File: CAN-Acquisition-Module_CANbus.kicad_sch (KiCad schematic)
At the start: 20 parts, among them J5 OSTVN04A150, J6 OSTVN04A150, U4 SN65HVD234

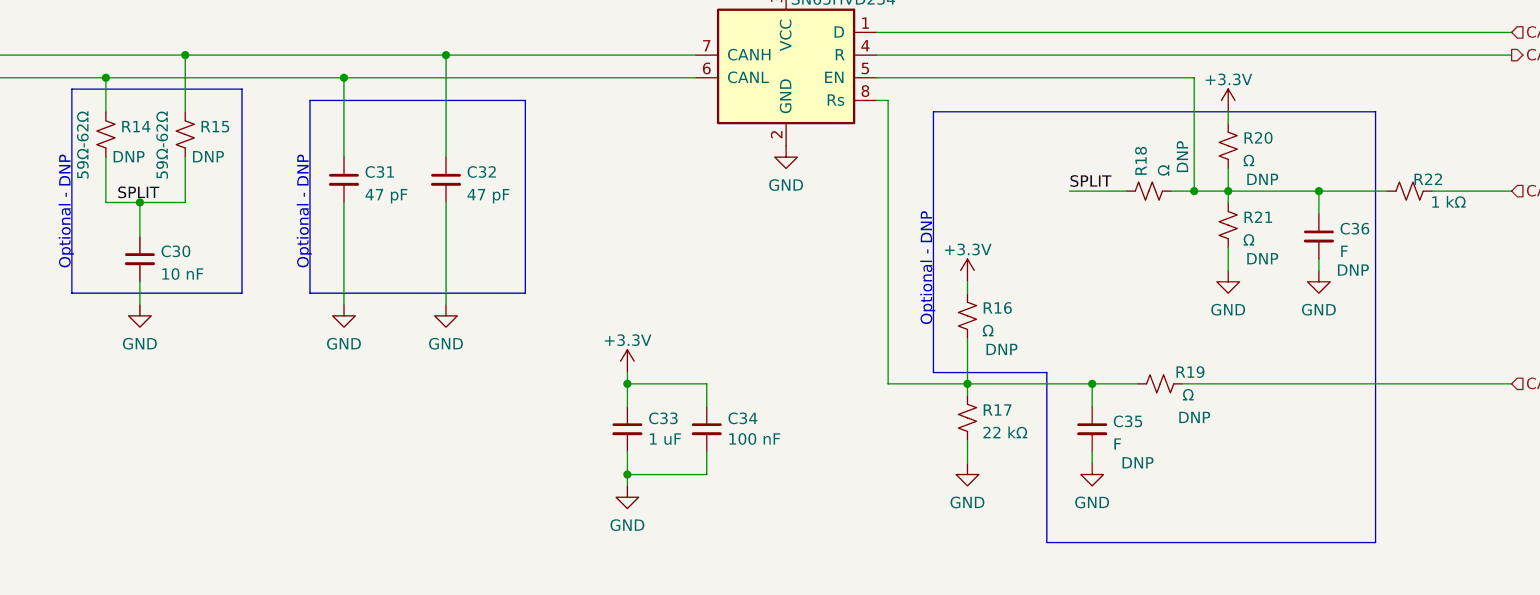
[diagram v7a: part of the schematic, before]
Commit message: Layout of analog section started
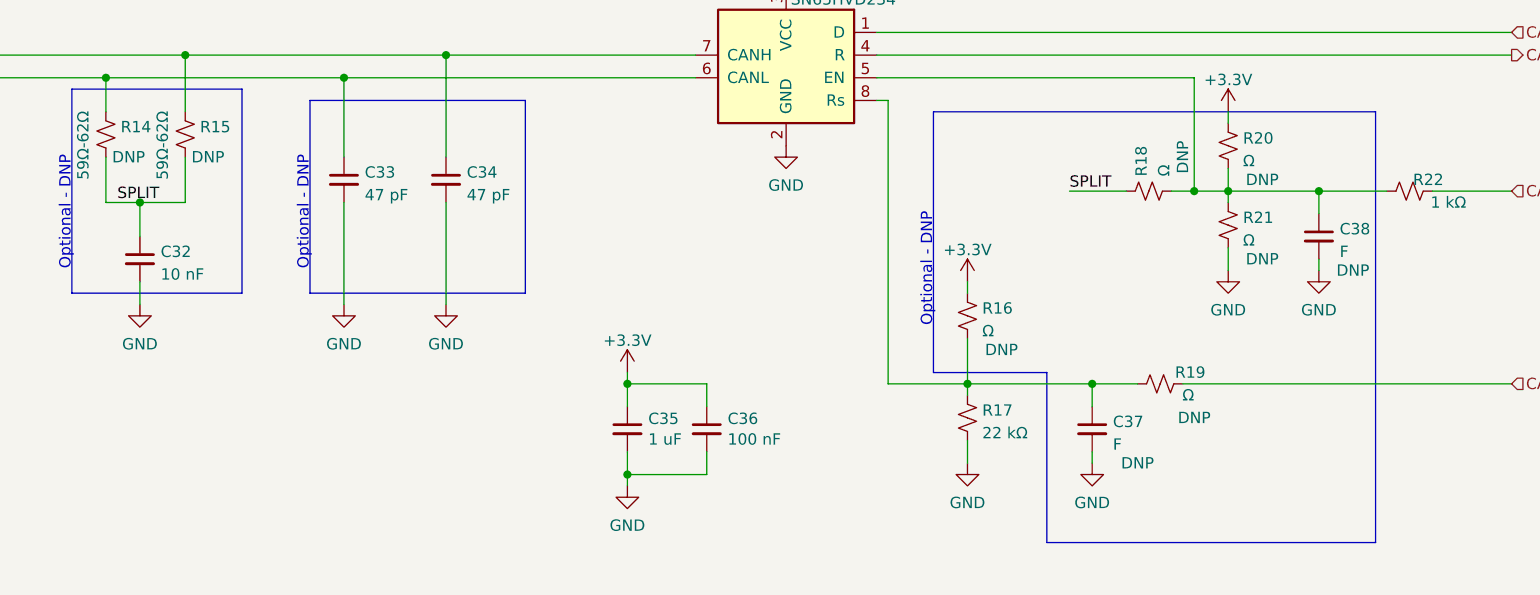
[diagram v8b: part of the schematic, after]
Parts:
- renumbered C30 to C32, C31 to C33, C32 to C34, C33 to C35, C34 to C36, C35 to C37, C36 to C38
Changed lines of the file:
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@@
   (symbol (lib_id "power:GND") (at 156.21 130.81 0) (unit 1)
     (in_bom yes) (on_board yes) (fields_autoplaced)
-    (property "Reference" "#PWR067" (id 0) (at 156.21 137.16 0)
+    (property "Reference" "#PWR069" (id 0) (at 156.21 137.16 0)
       (effects (font (size 1.27 1.27)) hide)
     )
@@
   (symbol (lib_id "power:+3.3V") (at 194.31 107.95 0) (unit 1)
     (in_bom yes) (on_board yes) (fields_autoplaced)
-    (property "Reference" "#PWR070" (id 0) (at 194.31 111.76 0)
+    (property "Reference" "#PWR072" (id 0) (at 194.31 111.76 0)
       (effects (font (size 1.27 1.27)) hide)
     )
@@
   (symbol (lib_id "power:GND") (at 173.99 92.71 0) (unit 1)
     (in_bom yes) (on_board yes)
-    (property "Reference" "#PWR069" (id 0) (at 173.99 99.06 0)
+    (property "Reference" "#PWR071" (id 0) (at 173.99 99.06 0)
       (effects (font (size 1.27 1.27)) hide)
     )
@@
   (symbol (lib_id "Device:C_Small") (at 135.89 96.52 0) (unit 1)
     (in_bom yes) (on_board yes) (fields_autoplaced)
-    (property "Reference" "C32" (id 0) (at 138.2141 95.6916 0)
+    (property "Reference" "C34" (id 0) (at 138.2141 95.6916 0)
       (effects (font (size 1.27 1.27)) (justify left))
     )
@@
   (symbol (lib_id "power:GND") (at 233.68 106.68 0) (unit 1)
     (in_bom yes) (on_board yes) (fields_autoplaced)
-    (property "Reference" "#PWR075" (id 0) (at 233.68 113.03 0)
+    (property "Reference" "#PWR077" (id 0) (at 233.68 113.03 0)
       (effects (font (size 1.27 1.27)) hide)
     )
@@
   (symbol (lib_id "Device:C_Small") (at 165.1 124.46 0) (unit 1)
     (in_bom yes) (on_board yes)
-    (property "Reference" "C34" (id 0) (at 167.4368 123.2916 0)
+    (property "Reference" "C36" (id 0) (at 167.4368 123.2916 0)
       (effects (font (size 1.27 1.27)) (justify left))
     )
@@
   (symbol (lib_id "power:GND") (at 41.91 71.12 0) (unit 1)
     (in_bom yes) (on_board yes) (fields_autoplaced)
-    (property "Reference" "#PWR061" (id 0) (at 41.91 77.47 0)
+    (property "Reference" "#PWR063" (id 0) (at 41.91 77.47 0)
       (effects (font (size 1.27 1.27)) hide)
     )
@@
   (symbol (lib_id "Device:C_Small") (at 156.21 124.46 0) (unit 1)
     (in_bom yes) (on_board yes)
-    (property "Reference" "C33" (id 0) (at 158.5468 123.2916 0)
+    (property "Reference" "C35" (id 0) (at 158.5468 123.2916 0)
       (effects (font (size 1.27 1.27)) (justify left))
     )
@@
   (symbol (lib_id "power:GND") (at 67.31 97.79 0) (unit 1)
     (in_bom yes) (on_board yes) (fields_autoplaced)
-    (property "Reference" "#PWR062" (id 0) (at 67.31 104.14 0)
+    (property "Reference" "#PWR064" (id 0) (at 67.31 104.14 0)
       (effects (font (size 1.27 1.27)) hide)
     )
@@
   (symbol (lib_id "Device:C_Small") (at 233.68 102.87 0) (unit 1)
     (in_bom yes) (on_board yes)
-    (property "Reference" "C36" (id 0) (at 236.0041 102.0416 0)
+    (property "Reference" "C38" (id 0) (at 236.0041 102.0416 0)
       (effects (font (size 1.27 1.27)) (justify left))
     )
@@
   (symbol (lib_id "power:+3.3V") (at 156.21 118.11 0) (unit 1)
     (in_bom yes) (on_board yes) (fields_autoplaced)
-    (property "Reference" "#PWR066" (id 0) (at 156.21 121.92 0)
+    (property "Reference" "#PWR068" (id 0) (at 156.21 121.92 0)
       (effects (font (size 1.27 1.27)) hide)
     )
@@
   (symbol (lib_id "Device:C_Small") (at 208.28 124.46 0) (unit 1)
     (in_bom yes) (on_board yes)
-    (property "Reference" "C35" (id 0) (at 210.6041 123.6316 0)
+    (property "Reference" "C37" (id 0) (at 210.6041 123.6316 0)
       (effects (font (size 1.27 1.27)) (justify left))
     )
@@
   (symbol (lib_id "Device:C_Small") (at 124.46 96.52 0) (unit 1)
     (in_bom yes) (on_board yes) (fields_autoplaced)
-    (property "Reference" "C31" (id 0) (at 126.7841 95.6916 0)
+    (property "Reference" "C33" (id 0) (at 126.7841 95.6916 0)
       (effects (font (size 1.27 1.27)) (justify left))
     )
@@
   (symbol (lib_id "power:GND") (at 101.6 110.49 0) (unit 1)
     (in_bom yes) (on_board yes) (fields_autoplaced)
-    (property "Reference" "#PWR063" (id 0) (at 101.6 116.84 0)
+    (property "Reference" "#PWR065" (id 0) (at 101.6 116.84 0)
       (effects (font (size 1.27 1.27)) hide)
     )
@@
   (symbol (lib_id "power:GND") (at 208.28 128.27 0) (unit 1)
     (in_bom yes) (on_board yes) (fields_autoplaced)
-    (property "Reference" "#PWR072" (id 0) (at 208.28 134.62 0)
+    (property "Reference" "#PWR074" (id 0) (at 208.28 134.62 0)
       (effects (font (size 1.27 1.27)) hide)
     )
@@
   (symbol (lib_id "Device:C_Small") (at 101.6 105.41 0) (unit 1)
     (in_bom yes) (on_board yes) (fields_autoplaced)
-    (property "Reference" "C30" (id 0) (at 103.9241 104.5816 0)
+    (property "Reference" "C32" (id 0) (at 103.9241 104.5816 0)
       (effects (font (size 1.27 1.27)) (justify left))
     )
@@
   (symbol (lib_id "power:GND") (at 135.89 110.49 0) (unit 1)
     (in_bom yes) (on_board yes) (fields_autoplaced)
-    (property "Reference" "#PWR065" (id 0) (at 135.89 116.84 0)
+    (property "Reference" "#PWR067" (id 0) (at 135.89 116.84 0)
       (effects (font (size 1.27 1.27)) hide)
     )
@@
   (symbol (lib_id "power:+3.3V") (at 173.99 74.93 0) (unit 1)
     (in_bom yes) (on_board yes) (fields_autoplaced)
-    (property "Reference" "#PWR068" (id 0) (at 173.99 78.74 0)
+    (property "Reference" "#PWR070" (id 0) (at 173.99 78.74 0)
       (effects (font (size 1.27 1.27)) hide)
     )
@@
   (symbol (lib_id "power:+3.3V") (at 223.52 88.9 0) (unit 1)
     (in_bom yes) (on_board yes) (fields_autoplaced)
-    (property "Reference" "#PWR073" (id 0) (at 223.52 92.71 0)
+    (property "Reference" "#PWR075" (id 0) (at 223.52 92.71 0)
       (effects (font (size 1.27 1.27)) hide)
     )
@@
   (symbol (lib_id "power:GND") (at 194.31 128.27 0) (unit 1)
     (in_bom yes) (on_board yes) (fields_autoplaced)
-    (property "Reference" "#PWR071" (id 0) (at 194.31 134.62 0)
+    (property "Reference" "#PWR073" (id 0) (at 194.31 134.62 0)
       (effects (font (size 1.27 1.27)) hide)
     )
@@
   (symbol (lib_id "power:GND") (at 124.46 110.49 0) (unit 1)
     (in_bom yes) (on_board yes) (fields_autoplaced)
-    (property "Reference" "#PWR064" (id 0) (at 124.46 116.84 0)
+    (property "Reference" "#PWR066" (id 0) (at 124.46 116.84 0)
       (effects (font (size 1.27 1.27)) hide)
     )
@@
   (symbol (lib_id "power:GND") (at 223.52 106.68 0) (unit 1)
     (in_bom yes) (on_board yes) (fields_autoplaced)
-    (property "Reference" "#PWR074" (id 0) (at 223.52 113.03 0)
-      (effects (font (size 1.27 1.27)) hide)
-    )
+    (property "Reference" "#PWR076" (id 0) (at 223.52 113.03 0)
+      (effects (font (size 1.27 1.27)) hide)
+    )
